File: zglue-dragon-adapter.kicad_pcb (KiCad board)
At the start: 8 copper layers, 25 x 20 mm, 56 parts, among them J1 543630489, J2 543630489, U1 zGlue-Dragon

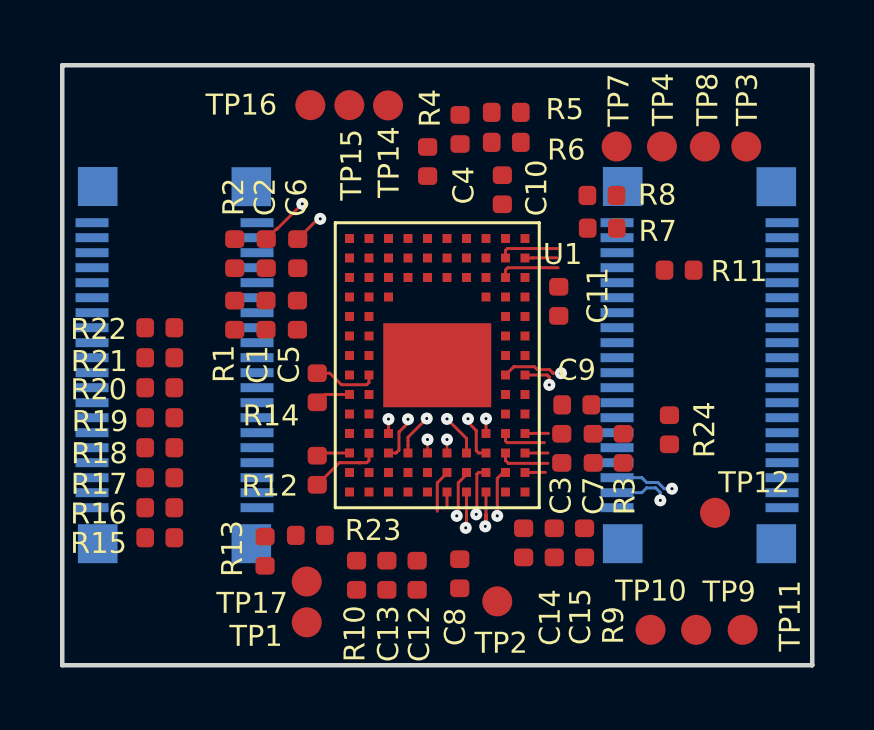
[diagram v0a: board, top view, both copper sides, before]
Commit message: Moved some capacitors and resistors away from LGA-96 chip
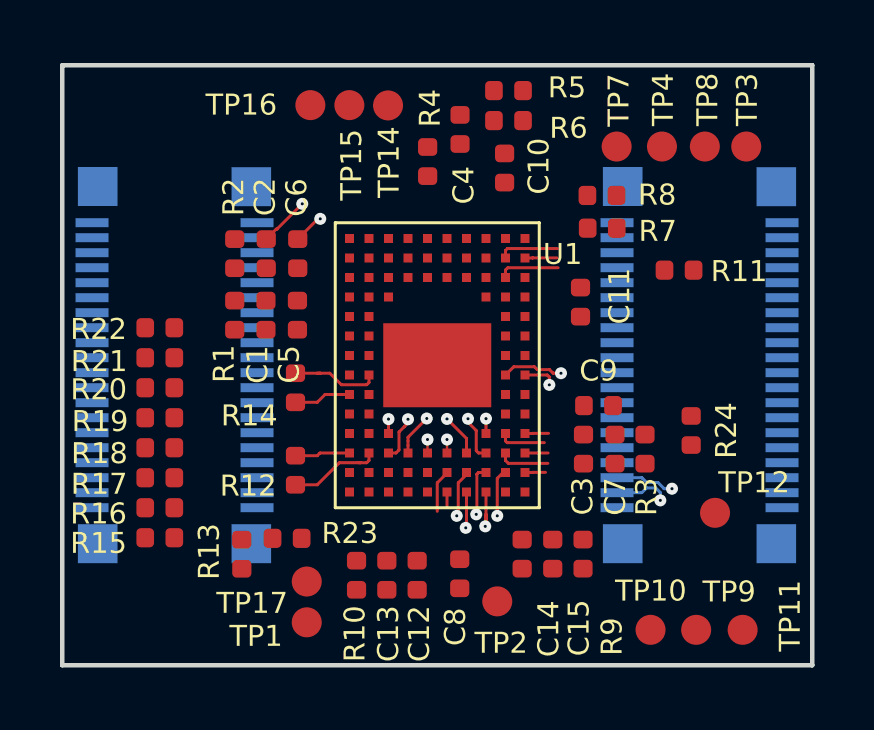
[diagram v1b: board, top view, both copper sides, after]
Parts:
- moved R13 0.78 mm to (5.99, 16.3)
- moved R23 0.78 mm to (7.50, 15.8)
- moved C10 0.73 mm to (14.7, 3.42)
- moved R5 0.73 mm to (14.9, 0.84)
- moved R6 0.73 mm to (14.9, 1.84)
- moved C3 0.73 mm to (17.4, 12.8)
- moved C7 0.73 mm to (18.4, 12.8)
- moved C9 0.73 mm to (17.9, 11.3)
- moved R24 0.73 mm to (21.0, 12.2)
- moved R3 0.73 mm to (19.4, 12.8)
- moved C11 0.73 mm to (17.3, 7.89)
- moved R12 0.72 mm to (7.78, 13.5)
- moved R14 0.72 mm to (7.78, 10.8)
- moved C14 0.38 mm to (15.3, 16.3)
- moved R9 0.38 mm to (17.4, 16.3)
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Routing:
- net /CSI_D2_FP_P: track 2.17 -> 2.99 mm
- net /CSI_D2_FP_N: track 1.20 -> 1.92 mm
- net /CSI_D1_FP_P: track 3.03 -> 3.75 mm
- net /CSI_D1_FP_N: track 1.11 -> 1.84 mm
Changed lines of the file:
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@@
     (thickness 1)
     (drawings 4)
-    (tracks 151)
+    (tracks 156)
     (zones 0)
     (modules 56)
@@
     (0 Top_Layer signal)
     (1 Power_Layer1 signal)
-    (2 Signal_Layer1 signal)
-    (3 Ground_Layer1 signal)
-    (4 Power_Layer2 signal)
-    (5 Signal_Layer2 signal)
-    (6 Ground_Layer2 signal)
+    (2 Signal_Layer1 signal hide)
+    (3 Ground_Layer1 signal hide)
+    (4 Power_Layer2 signal hide)
+    (5 Signal_Layer2 signal hide)
+    (6 Ground_Layer2 signal hide)
     (31 Bottom_Layer signal)
     (32 B.Adhes user)
@@
   )
   (module antmicro-footprints:0402-cap (layer Top_Layer)
-    (at 17.7 12.77 270)
+    (at 18.425 12.795 270)
     (descr "Resistor SMD 0402 (1005 Metric), square (rectangular) end terminal, IPC_7351 nominal, (Body size source: http://www.tortai-tech.com/upload/download/2011102023233369053.pdf), generated with kicad-footprint-generator")
     (tags resistor)
@@
   )
   (module antmicro-footprints:0402-cap (layer Top_Layer)
-    (at 16.65 12.77 270)
+    (at 17.375 12.795 270)
     (descr "Resistor SMD 0402 (1005 Metric), square (rectangular) end terminal, IPC_7351 nominal, (Body size source: http://www.tortai-tech.com/upload/download/2011102023233369053.pdf), generated with kicad-footprint-generator")
     (tags resistor)
@@
   )
   (module antmicro-footprints:0402-cap (layer Top_Layer)
-    (at 14.67 4.15 90)
+    (at 14.745 3.425 90)
     (descr "Resistor SMD 0402 (1005 Metric), square (rectangular) end terminal, IPC_7351 nominal, (Body size source: http://www.tortai-tech.com/upload/download/2011102023233369053.pdf), generated with kicad-footprint-generator")
     (tags resistor)
@@
   )
   (module antmicro-footprints:0402-cap (layer Top_Layer)
-    (at 15.38 15.92 270)
+    (at 15.33 16.295 270)
     (descr "Resistor SMD 0402 (1005 Metric), square (rectangular) end terminal, IPC_7351 nominal, (Body size source: http://www.tortai-tech.com/upload/download/2011102023233369053.pdf), generated with kicad-footprint-generator")
     (tags resistor)
@@
   )
   (module antmicro-footprints:0402-res (layer Top_Layer)
-    (at 20.24 12.15 270)
+    (at 20.965 12.175 270)
     (descr "Resistor SMD 0402 (1005 Metric), square (rectangular) end terminal, IPC_7351 nominal, (Body size source: http://www.tortai-tech.com/upload/download/2011102023233369053.pdf), generated with kicad-footprint-generator")
     (tags resistor)
@@
   )
   (module antmicro-footprints:0402-res (layer Top_Layer)
-    (at 17.41 15.92 90)
+    (at 17.36 16.295 90)
     (descr "Resistor SMD 0402 (1005 Metric), square (rectangular) end terminal, IPC_7351 nominal, (Body size source: http://www.tortai-tech.com/upload/download/2011102023233369053.pdf), generated with kicad-footprint-generator")
     (tags resistor)
@@
   )
   (module antmicro-footprints:0402-res (layer Top_Layer)
-    (at 14.8 2.57)
+    (at 14.875 1.845)
     (descr "Resistor SMD 0402 (1005 Metric), square (rectangular) end terminal, IPC_7351 nominal, (Body size source: http://www.tortai-tech.com/upload/download/2011102023233369053.pdf), generated with kicad-footprint-generator")
     (tags resistor)
@@
   )
   (module antmicro-footprints:0402-res (layer Top_Layer)
-    (at 14.8 1.57)
+    (at 14.875 0.845)
     (descr "Resistor SMD 0402 (1005 Metric), square (rectangular) end terminal, IPC_7351 nominal, (Body size source: http://www.tortai-tech.com/upload/download/2011102023233369053.pdf), generated with kicad-footprint-generator")
     (tags resistor)
@@
   )
   (module antmicro-footprints:0402-res (layer Top_Layer)
-    (at 18.7 12.77 90)
+    (at 19.425 12.795 90)
     (descr "Resistor SMD 0402 (1005 Metric), square (rectangular) end terminal, IPC_7351 nominal, (Body size source: http://www.tortai-tech.com/upload/download/2011102023233369053.pdf), generated with kicad-footprint-generator")
     (tags resistor)
@@
   )
   (module antmicro-footprints:0402-res (layer Top_Layer)
-    (at 6.76 16.2 270)
+    (at 5.985 16.3 270)
     (descr "Resistor SMD 0402 (1005 Metric), square (rectangular) end terminal, IPC_7351 nominal, (Body size source: http://www.tortai-tech.com/upload/download/2011102023233369053.pdf), generated with kicad-footprint-generator")
     (tags resistor)
@@
   )
   (module antmicro-footprints:0402-cap (layer Top_Layer)
-    (at 16.4 15.92 270)
+    (at 16.35 16.295 270)
     (descr "Resistor SMD 0402 (1005 Metric), square (rectangular) end terminal, IPC_7351 nominal, (Body size source: http://www.tortai-tech.com/upload/download/2011102023233369053.pdf), generated with kicad-footprint-generator")
     (tags resistor)
@@
   )
   (module antmicro-footprints:0402-cap (layer Top_Layer)
-    (at 17.15 11.32)
+    (at 17.875 11.345)
     (descr "Resistor SMD 0402 (1005 Metric), square (rectangular) end terminal, IPC_7351 nominal, (Body size source: http://www.tortai-tech.com/upload/download/2011102023233369053.pdf), generated with kicad-footprint-generator")
     (tags resistor)
@@
   )
   (module antmicro-footprints:0402-cap (layer Top_Layer)
-    (at 16.55 7.87 90)
+    (at 17.275 7.895 90)
     (descr "Resistor SMD 0402 (1005 Metric), square (rectangular) end terminal, IPC_7351 nominal, (Body size source: http://www.tortai-tech.com/upload/download/2011102023233369053.pdf), generated with kicad-footprint-generator")
     (tags resistor)
@@
   )
   (module antmicro-footprints:0402-res (layer Top_Layer)
-    (at 8.27 15.67 180)
+    (at 7.495 15.77 180)
     (descr "Resistor SMD 0402 (1005 Metric), square (rectangular) end terminal, IPC_7351 nominal, (Body size source: http://www.tortai-tech.com/upload/download/2011102023233369053.pdf), generated with kicad-footprint-generator")
     (tags resistor)
@@
   )
   (module antmicro-footprints:0402-res (layer Top_Layer)
-    (at 8.5 10.75 270)
+    (at 7.775 10.75 270)
     (descr "Resistor SMD 0402 (1005 Metric), square (rectangular) end terminal, IPC_7351 nominal, (Body size source: http://www.tortai-tech.com/upload/download/2011102023233369053.pdf), generated with kicad-footprint-generator")
     (tags resistor)
@@
   )
   (module antmicro-footprints:0402-res (layer Top_Layer)
-    (at 8.5 13.5 90)
+    (at 7.775 13.5 90)
     (descr "Resistor SMD 0402 (1005 Metric), square (rectangular) end terminal, IPC_7351 nominal, (Body size source: http://www.tortai-tech.com/upload/download/2011102023233369053.pdf), generated with kicad-footprint-generator")
     (tags resistor)
@@
   (segment (start 14.85 6.75) (end 16.53 6.75) (width 0.1) (layer Top_Layer) (net 26))
   (segment (start 8.92 10.265) (end 9.305 10.65) (width 0.1) (layer Top_Layer) (net 46))
-  (segment (start 8.5 10.265) (end 8.92 10.265) (width 0.1) (layer Top_Layer) (net 46))
   (segment (start 10.15 10.65) (end 10.225 10.575) (width 0.1) (layer Top_Layer) (net 46))
   (segment (start 10.225 10.575) (end 10.225 10.325) (width 0.1) (layer Top_Layer) (net 46))
   (segment (start 9.305 10.65) (end 10.15 10.65) (width 0.1) (layer Top_Layer) (net 46))
+  (segment (start 8.6 10.265) (end 7.775 10.265) (width 0.1) (layer Top_Layer) (net 46))
+  (segment (start 8.5 10.265) (end 8.6 10.265) (width 0.1) (layer Top_Layer) (net 46))
+  (segment (start 8.6 10.265) (end 8.92 10.265) (width 0.1) (layer Top_Layer) (net 46))
   (via (at 16.624455 10.265545) (size 0.4) (drill 0.1) (layers Top_Layer Bottom_Layer) (net 47))
   (segment (start 16.362825 10.265545) (end 16.624455 10.265545) (width 0.1) (layer Top_Layer) (net 47))
@@
   (segment (start 8.76 10.975) (end 8.5 11.235) (width 0.1) (layer Top_Layer) (net 51))
   (segment (start 9.575 10.975) (end 8.76 10.975) (width 0.1) (layer Top_Layer) (net 51))
+  (segment (start 8.5 11.235) (end 7.775 11.235) (width 0.1) (layer Top_Layer) (net 51))
   (via (at 10.875 11.795) (size 0.4) (drill 0.1) (layers Top_Layer Bottom_Layer) (net 57))
   (segment (start 10.875 12.275) (end 10.875 11.8) (width 0.08) (layer Top_Layer) (net 57))
@@
   (segment (start 9.95 13.25) (end 9.875 13.25) (width 0.1) (layer Top_Layer) (net 64))
   (segment (start 9.235 13.25) (end 8.5 13.985) (width 0.1) (layer Top_Layer) (net 64))
+  (segment (start 8.5 13.985) (end 7.775 13.985) (width 0.1) (layer Top_Layer) (net 64))
   (segment (start 13.475 13.575) (end 13.475 13.645) (width 0.1) (layer Top_Layer) (net 65))
   (segment (start 13.475 13.645) (end 13.2 13.92) (width 0.1) (layer Top_Layer) (net 65))
@@
   (segment (start 8.59 12.925) (end 8.5 13.015) (width 0.1) (layer Top_Layer) (net 70))
   (segment (start 9.575 12.925) (end 8.59 12.925) (width 0.1) (layer Top_Layer) (net 70))
+  (segment (start 8.5 13.015) (end 7.775 13.015) (width 0.1) (layer Top_Layer) (net 70))
   (via (at 12.825 12.475) (size 0.4) (drill 0.1) (layers Top_Layer Bottom_Layer) (net 71))
   (segment (start 12.825 12.925) (end 12.825 12.475) (width 0.08) (layer Top_Layer) (net 71))

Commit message: Rotated PCB by 180 deg to match chip logo orientation
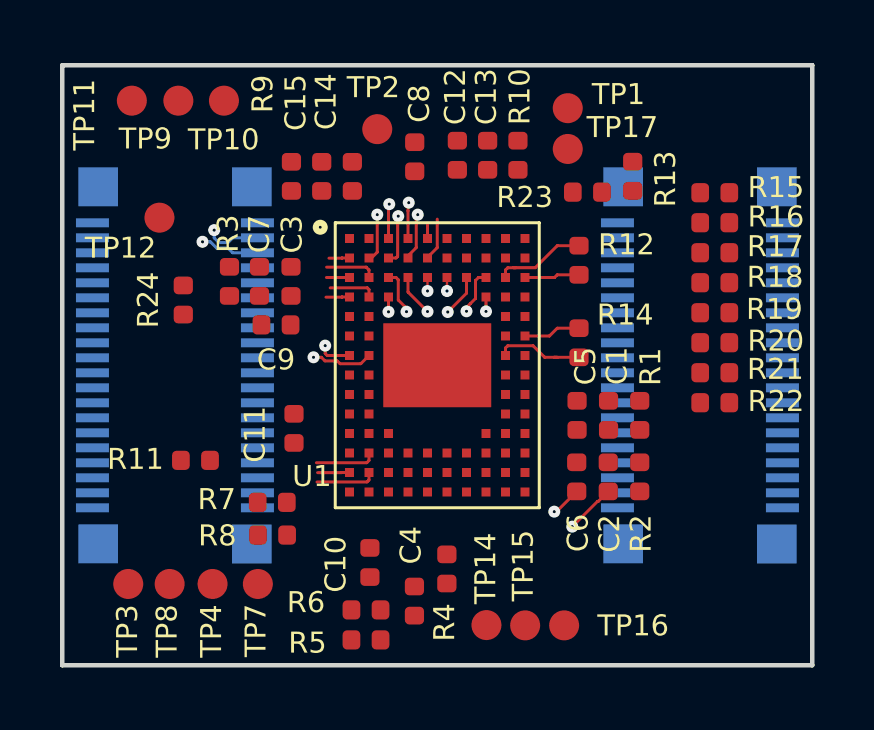
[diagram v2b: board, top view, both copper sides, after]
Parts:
- moved TP11 27.0 mm to (2.32, 1.13), turned to 180 degrees
- moved TP3 25.2 mm to (2.20, 17.2), turned to 180 degrees
- moved TP9 24.8 mm to (3.87, 1.13), turned to 180 degrees
- moved TP8 23.0 mm to (3.58, 17.2), turned to 180 degrees
- moved TP10 22.7 mm to (5.39, 1.13), turned to 180 degrees
- moved R15 21.8 mm to (21.8, 4.25), turned to 0 degrees
- moved TP12 21.0 mm to (3.24, 5.03), turned to 180 degrees
- moved TP4 20.8 mm to (5.01, 17.2), turned to 180 degrees
- moved R16 20.8 mm to (21.8, 5.25), turned to 0 degrees
- moved R17 20.0 mm to (21.8, 6.25), turned to 0 degrees
- moved TP1 19.3 mm to (16.9, 1.38), turned to 180 degrees
- moved R18 19.3 mm to (21.8, 7.25), turned to 0 degrees
- moved TP16 19.2 mm to (16.7, 18.6), turned to 180 degrees
- moved R5 18.9 mm to (10.1, 19.2), turned to 180 degrees
- moved R19 18.8 mm to (21.8, 8.25), turned to 0 degrees
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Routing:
- net GND: track 4.73 -> 25.8 mm
- net /CSI_CLK_IN_N: track 14.0 -> 3.08 mm
- net /CSI_CLK_IN_P: track 14.1 -> 3.89 mm

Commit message: Changed PCB stackup to 6-layer, added stackup table, changed design rules
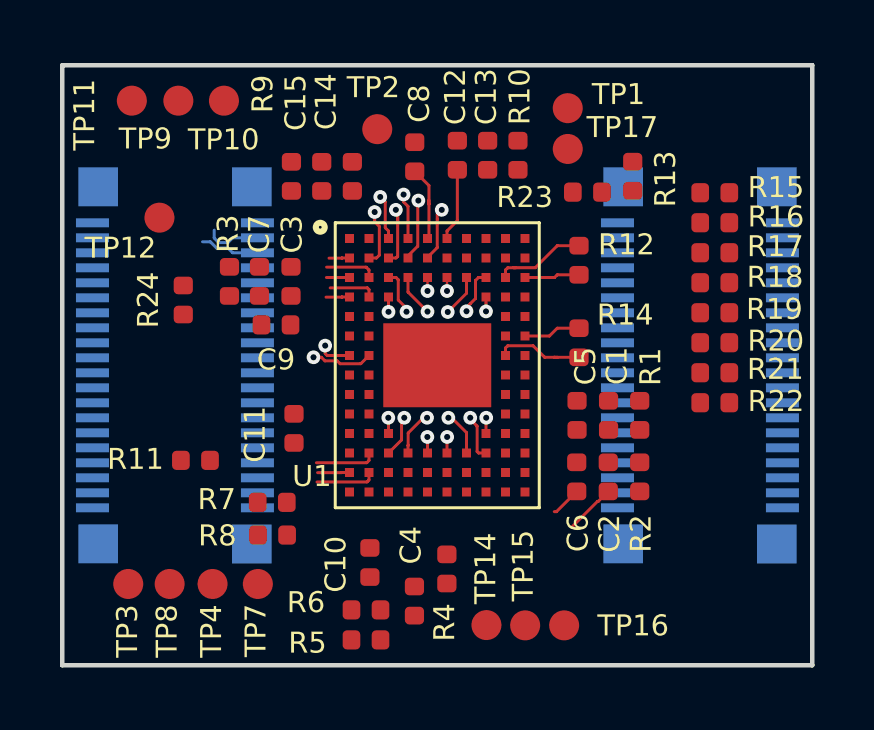
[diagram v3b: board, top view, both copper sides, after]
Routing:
- net GND: track 25.8 -> 4.73 mm, vias 2 -> 0
- net /VPLL_B: track 0.00 -> 2.43 mm
- net /1V2_SYS_B: track 0.52 -> 2.59 mm
- net /TMS: track 0.00 -> 1.49 mm, vias 0 -> 1
- net Net-(U1-PadM3): track 0.00 -> 1.35 mm, vias 0 -> 1
- net /VSENSE: track 0.00 -> 1.30 mm, vias 0 -> 1
- net /LED3_ISINK: track 0.00 -> 1.30 mm, vias 0 -> 1
- net /LED2_ISINK: track 0.00 -> 0.56 mm, vias 0 -> 1
- net /LED1_ISINK: track 0.00 -> 0.54 mm, vias 0 -> 1
- net /EXTCLK_EN: track 0.00 -> 0.51 mm, vias 0 -> 1
- net /TDO: track 0.00 -> 0.49 mm, vias 0 -> 1
- net /PROC_SO: track 1.43 -> 1.80 mm, vias 0 -> 1
- net /CSI_CLK_IN_P: vias 2 -> 1
- net /CSI_CLK_IN_N: vias 2 -> 1
- removed copper zone on Power_Layer2, net /1V2_SYS
- removed copper zone on Power_Layer1, net /3V3_SYS
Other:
- copper layers 8 -> 6
- net class Default: via_dia 0.4 -> 0.457; via_drill 0.1 -> 0.2
- rule via_min_size: 0.4 -> 0.457
- board text added: "0.02mm"
- board text added: "0.035mm"
- board text added: "0.12"
- board text added: "0.12mm"
- board text added: "0.14"
- board text added: "0.2"
- board text added: "1"
- board text added: "3.5"
- board text added: "4.2"
- board text added: "Bottom Layer"
- board text added: "Bottom Solder"
- board text added: "Constant"
- board text added: "Copper"
- board text added: "Core 1"
- board text added: "Core 2"
- board text added: "Dielectric 1"
- board text added: "Dielectric 3"
- board text added: "Dielectric2"
- board text added: "FR-4"
- board text added: "Ground Plane 1"
- board text added: "Ground Plane 2"
- board text added: "Layer"
- board text added: "Material"
- board text added: "Name"
- board text added: "Signal Layer 1"
- board text added: "Signal Layer 2"
- board text added: "Solder Resist"
- board text added: "Thickness"
- board text added: "Top Layer"
- board text added: "Top Solder"

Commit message: Routing finished
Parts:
- moved R11 2.71 mm to (3.67, 15.8), turned to 90 degrees
- moved R19 1.59 mm to (21.4, 9.81)
- moved R20 1.59 mm to (21.4, 10.8)
- moved R21 1.59 mm to (21.4, 11.8)
- moved R22 1.59 mm to (21.4, 12.8)
- moved TP12 1.47 mm to (2.53, 3.74)
- moved R24 1.29 mm to (3.80, 6.56)
- moved C6 0.82 mm to (17.9, 14.1)
- moved C2 0.82 mm to (18.9, 14.1)
- moved R2 0.82 mm to (19.9, 14.1)
- moved C4 0.76 mm to (11.8, 18.6)
- moved R16 0.75 mm to (21.4, 4.56)
- moved R17 0.75 mm to (21.4, 5.56)
- moved R18 0.75 mm to (21.4, 6.56)
- moved R15 0.75 mm to (21.4, 3.56)
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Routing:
- net /3V3_SYS: track 0.69 -> 72.9 mm, vias 0 -> 7
- net GND: track 4.73 -> 72.3 mm, vias 0 -> 42
- net /1V2_SYS: track 0.00 -> 54.5 mm, vias 0 -> 3
- net /CTRL_SO: track 0.00 -> 49.4 mm, vias 0 -> 2
- net /1V2_SYS_B: track 2.59 -> 49.8 mm, vias 0 -> 3
- net /CTRL_SCK: track 0.00 -> 44.8 mm, vias 0 -> 4
- net /CTRL_SI: track 0.00 -> 43.2 mm, vias 0 -> 2
- net /CTRL_SS: track 0.77 -> 43.8 mm, vias 0 -> 3
- net /3V3: track 0.00 -> 39.6 mm, vias 0 -> 5
- net /TCK: track 0.00 -> 39.0 mm, vias 0 -> 2
- net /2V5: track 0.00 -> 34.9 mm, vias 0 -> 4
- net /TDI: track 0.00 -> 34.8 mm, vias 0 -> 2
- net /1V8_SYS: track 0.00 -> 32.4 mm, vias 0 -> 2
- net /I2C_1_SDA: track 0.00 -> 30.9 mm, vias 0 -> 2
- net /LED3_ISINK: track 1.30 -> 30.7 mm, vias 1 -> 3
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- removed copper zone on Ground_Layer1, net GND

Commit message: Added second ground plane, updated gerbers
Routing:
- added copper zone on Ground_Layer1, net GND
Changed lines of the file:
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@@
   (layers
     (0 Top_Layer mixed)
-    (1 Ground_Layer1 signal hide)
+    (1 Ground_Layer1 signal)
     (2 Signal_Layer1 signal)
     (3 Signal_Layer2 signal)
-    (4 Ground_Layer2 signal hide)
+    (4 Ground_Layer2 signal)
     (31 Bottom_Layer signal)
     (32 B.Adhes user hide)
@@
     (visible_elements FFFFFF7F)
     (pcbplotparams
-      (layerselection 0x0d0fc_ffffffff)
+      (layerselection 0x0d1fc_ffffffff)
       (usegerberextensions false)
       (usegerberattributes false)
@@
       )
     )
+  )
+  (zone (net 2) (net_name GND) (layer Ground_Layer1) (hatch edge 0.508)
+    (connect_pads (clearance 0.1))
+    (min_thickness 0.254)
+    (fill yes (arc_segments 16) (thermal_gap 0.508) (thermal_bridge_width 0.508))
+    (polygon
+      (pts
+        (xy 24.99 -0.02) (xy 0.04 0.01) (xy 0.1 20.06) (xy 25.02 19.9)
+      )
+    )
